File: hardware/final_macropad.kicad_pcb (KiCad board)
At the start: 4 copper layers, 91.2 x 120.5 mm, 69 parts, among them J2 2137160001, SW1 SW_Push, U1 ATmega32U4-A, U2 USBLC6-2SC6, U3 DM-OLED096-636, Y1 16MHz

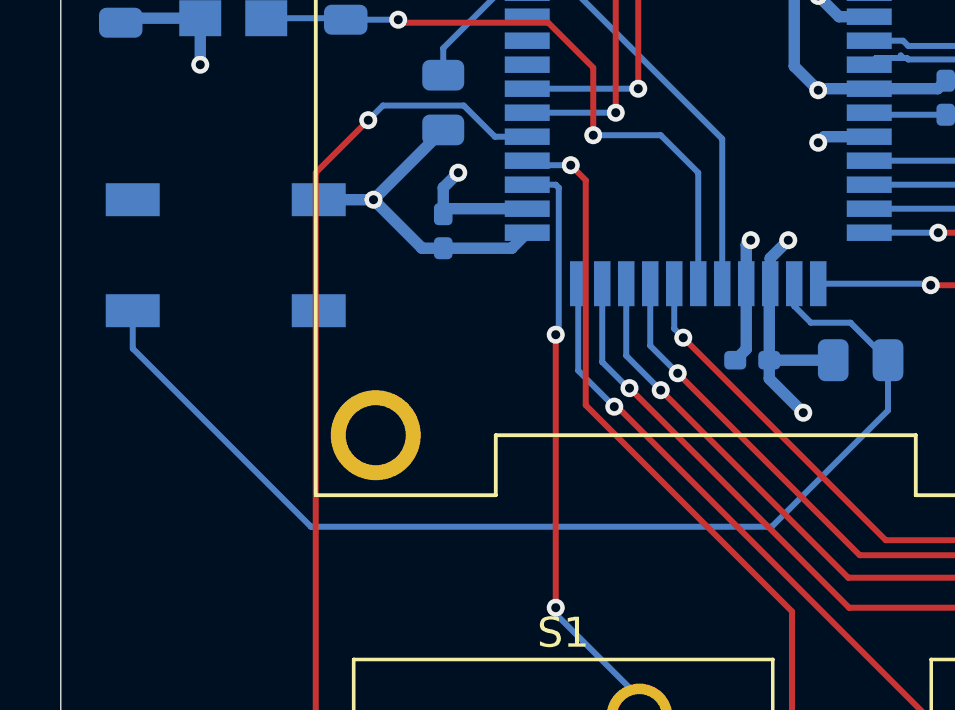
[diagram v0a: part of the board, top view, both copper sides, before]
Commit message: update BOM and reset button footprint
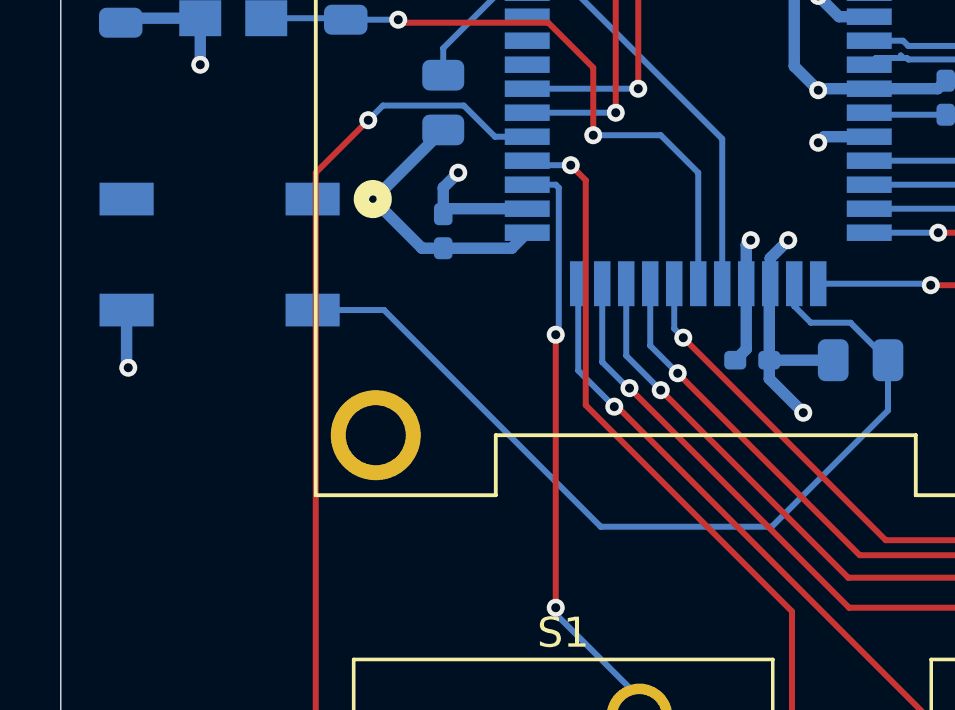
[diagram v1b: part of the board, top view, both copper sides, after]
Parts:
- SW1: value SW_Push -> SKQGADE010; footprint random-keyboard-parts:SKQG-1155865 -> Low_Profile_switch:SKQGADE010_AAL
- moved SW1 0.21 mm to (33.8, 49.0), turned to 180 degrees
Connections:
- SW1 pad 1: GND -> unconnected-(SW1-Pad1)
- SW1 pad 2: Net-(U1-~{RESET}) -> unconnected-(SW1-Pad2)
- SW1 pad 3: (no net) -> Net-(U1-~{RESET})
- SW1 pad 4: (no net) -> GND
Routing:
- net Net-(U1-~{RESET}): track 36.8 -> 30.1 mm
- net GND: track 75.7 -> 75.8 mm, vias 10 -> 11

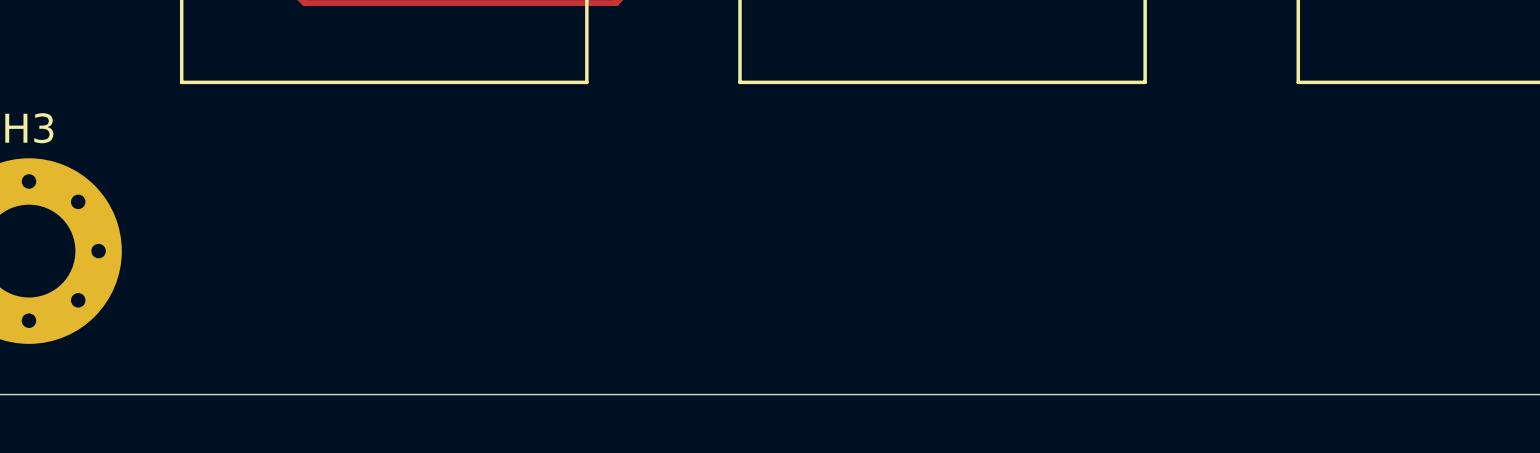
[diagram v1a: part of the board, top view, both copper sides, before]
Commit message: update BOM and add to silkscreen
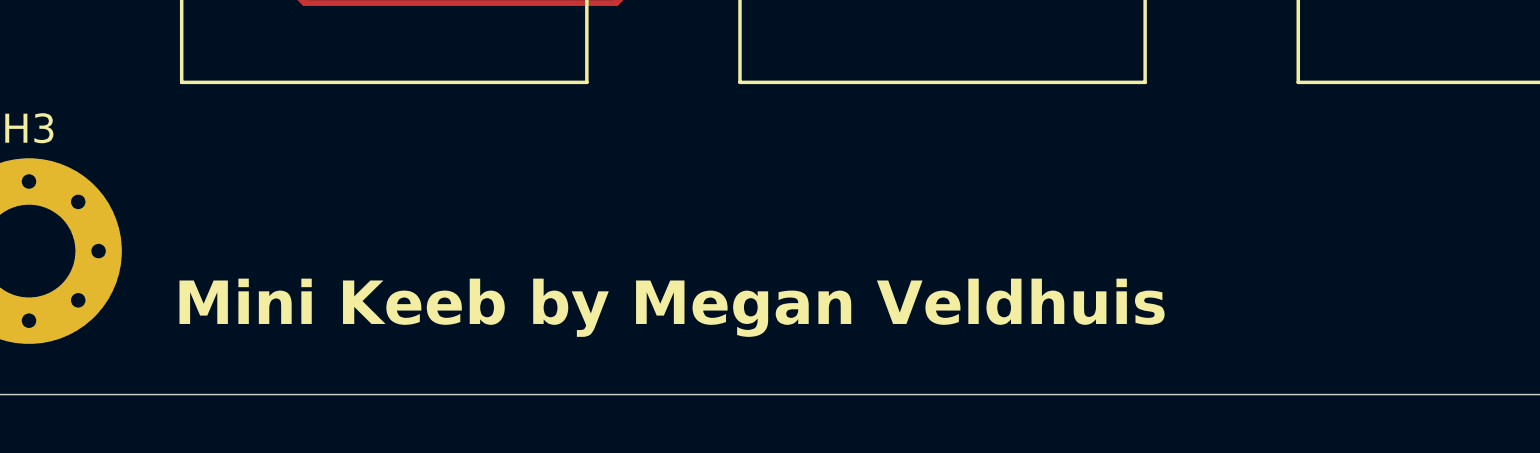
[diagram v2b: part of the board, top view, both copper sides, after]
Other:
- board text added: "Mini Keeb by Megan Veldhuis"
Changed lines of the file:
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@@
 		(layer "Edge.Cuts")
+	)
+	(gr_text "Mini Keeb by Megan Veldhuis"
+		(at 38 142.75 0)
+		(layer "F.SilkS")
+		(effects
+			(font
+				(size 1.5 1.5)
+				(thickness 0.3)
+				(bold yes)
+			)
+			(justify left bottom)
+		)
 	)
 	(segment
